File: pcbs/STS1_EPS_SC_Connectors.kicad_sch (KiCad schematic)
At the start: 15 parts, among them J2 Panel Y-, J4 Panel Y+, J5 Panel Z-, J6 Panel Z+, J7 Panel X+, U25 TPS259472ARPW

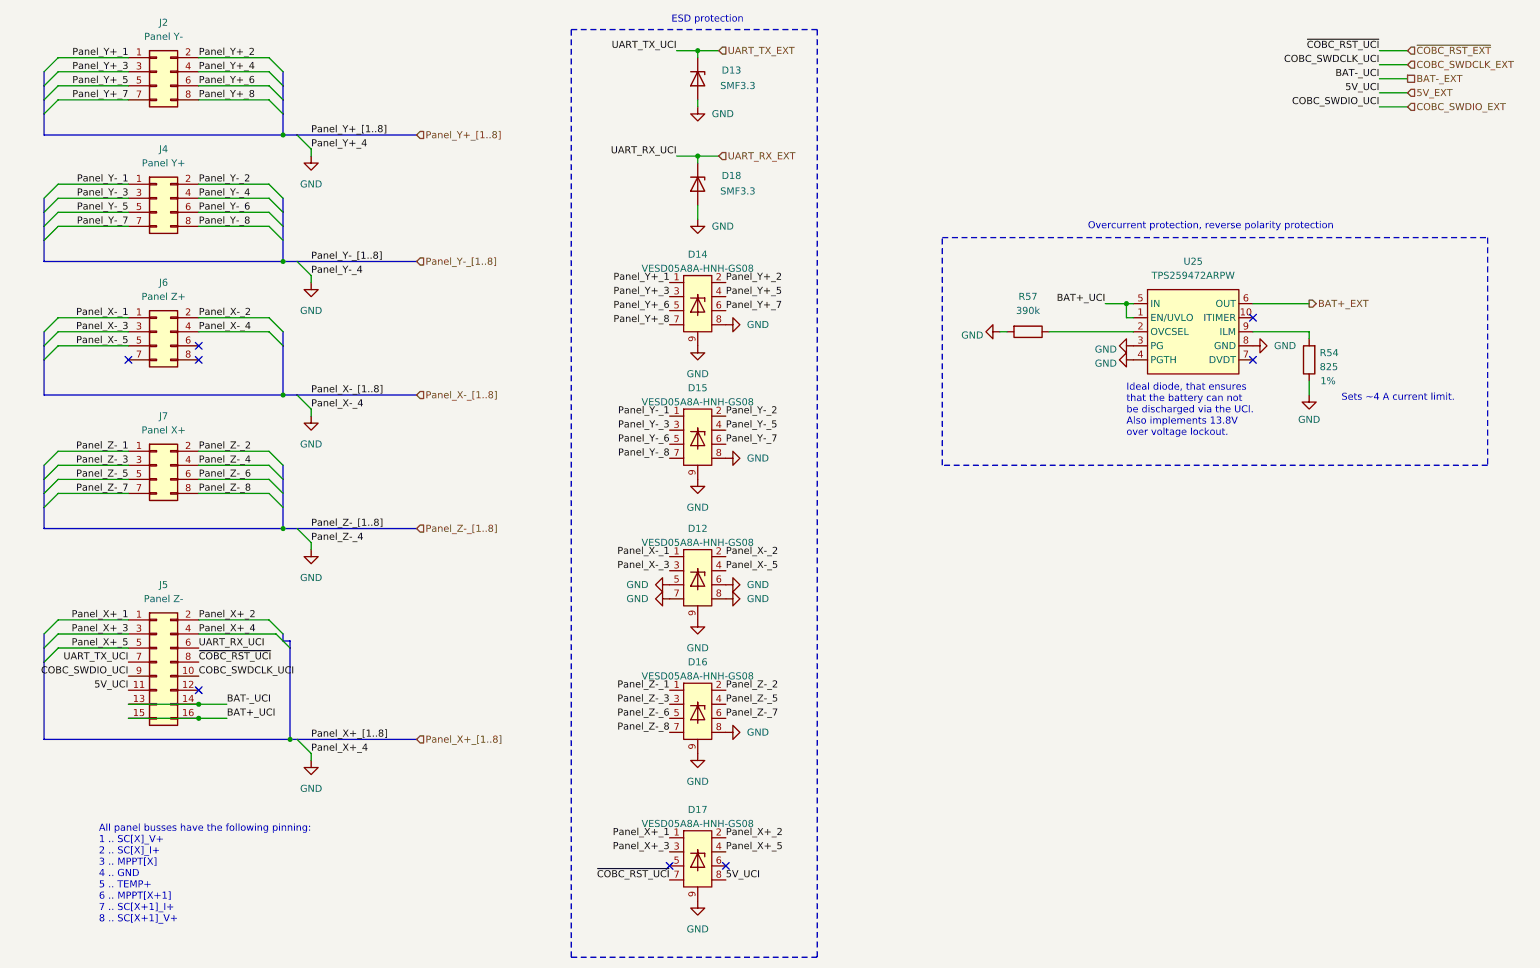
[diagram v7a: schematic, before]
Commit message: Added python script for replacing labels within KiCad.
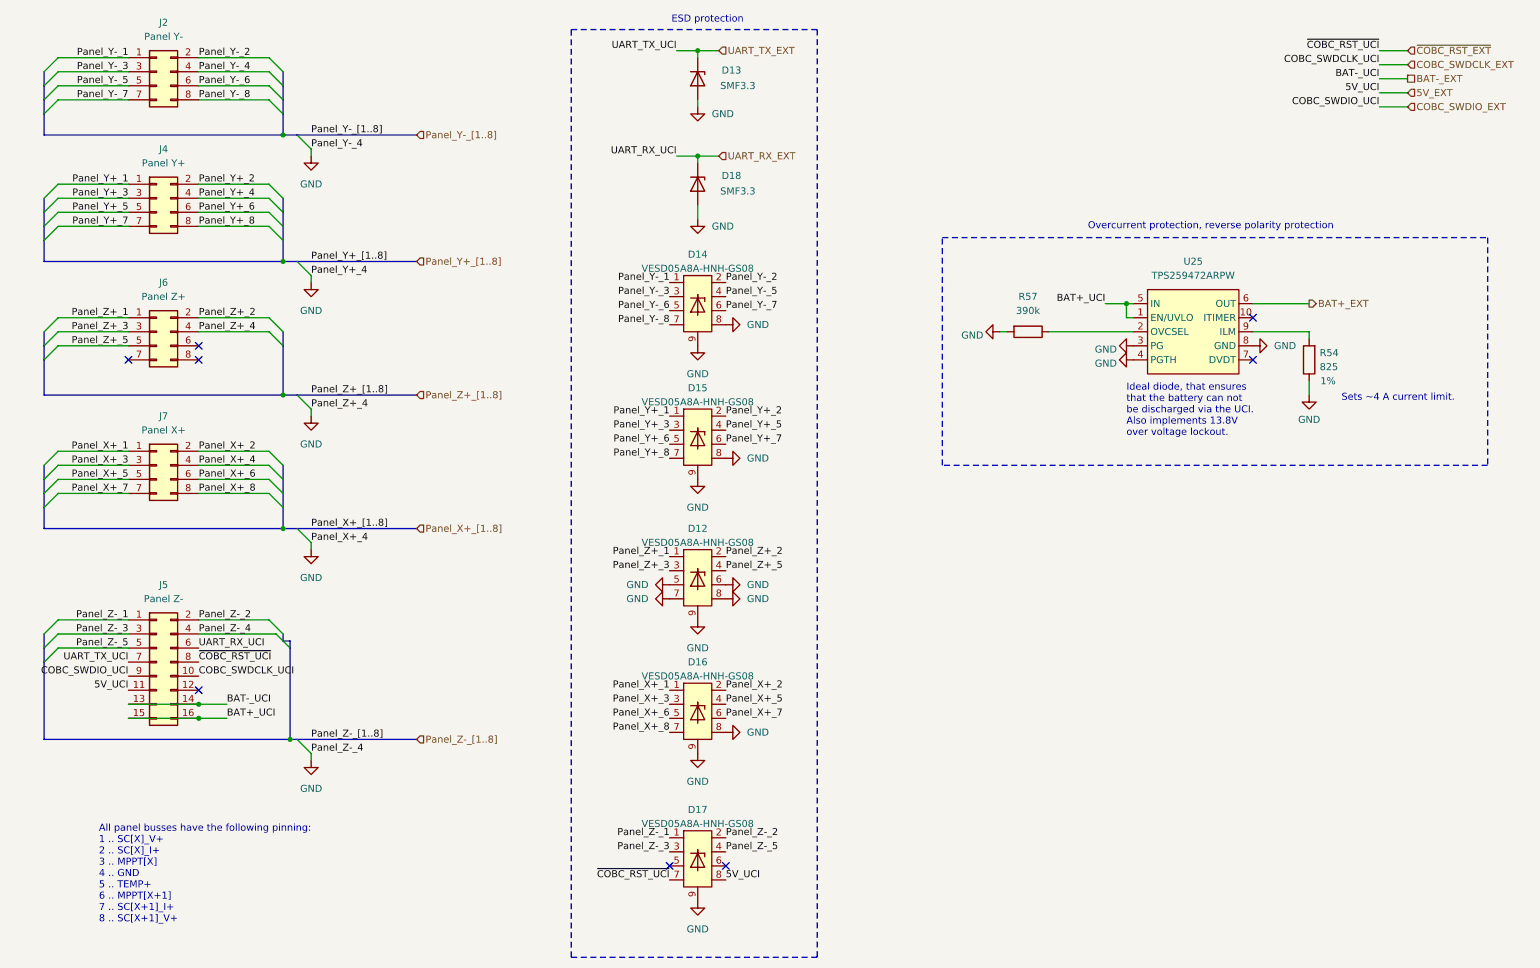
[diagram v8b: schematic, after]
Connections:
- net Panel_X+_1: now also D16.1, J7.1 (Pin_1); no longer D17.1, J5.1 (Pin_1)
- net Panel_X+_2: now also D16.2, J7.2 (Pin_2); no longer D17.2, J5.2 (Pin_2)
- net Panel_X+_3: now also D16.3, J7.3 (Pin_3); no longer D17.3, J5.3 (Pin_3)
- net Panel_X+_5: now also D16.4, J7.5 (Pin_5); no longer D17.4, J5.5 (Pin_5)
- net Panel_Y+_1: now also D15.1, J4.1 (Pin_1); no longer D14.1, J2.1 (Pin_1)
- net Panel_Y+_2: now also D15.2, J4.2 (Pin_2); no longer D14.2, J2.2 (Pin_2)
- net Panel_Y+_3: now also D15.3, J4.3 (Pin_3); no longer D14.3, J2.3 (Pin_3)
- net Panel_Y+_5: now also D15.4, J4.5 (Pin_5); no longer D14.4, J2.5 (Pin_5)
- net Panel_Y+_6: now also D15.5, J4.6 (Pin_6); no longer D14.5, J2.6 (Pin_6)
- net Panel_Y+_7: now also D15.6, J4.7 (Pin_7); no longer D14.6, J2.7 (Pin_7)
- net Panel_Y+_8: now also D15.7, J4.8 (Pin_8); no longer D14.7, J2.8 (Pin_8)
- net Panel_Y-_1: now also D14.1, J2.1 (Pin_1); no longer D15.1, J4.1 (Pin_1)
- net Panel_Y-_2: now also D14.2, J2.2 (Pin_2); no longer D15.2, J4.2 (Pin_2)
- net Panel_Y-_3: now also D14.3, J2.3 (Pin_3); no longer D15.3, J4.3 (Pin_3)
- net Panel_Y-_5: now also D14.4, J2.5 (Pin_5); no longer D15.4, J4.5 (Pin_5)
- net Panel_Y-_6: now also D14.5, J2.6 (Pin_6); no longer D15.5, J4.6 (Pin_6)
- net Panel_Y-_7: now also D14.6, J2.7 (Pin_7); no longer D15.6, J4.7 (Pin_7)
- net Panel_Y-_8: now also D14.7, J2.8 (Pin_8); no longer D15.7, J4.8 (Pin_8)
- net Panel_Z-_1: now also D17.1, J5.1 (Pin_1); no longer D16.1, J7.1 (Pin_1)
- net Panel_Z-_2: now also D17.2, J5.2 (Pin_2); no longer D16.2, J7.2 (Pin_2)
- net Panel_Z-_3: now also D17.3, J5.3 (Pin_3); no longer D16.3, J7.3 (Pin_3)
- net Panel_Z-_5: now also D17.4, J5.5 (Pin_5); no longer D16.4, J7.5 (Pin_5)
- net Panel_X-_1 renamed Panel_Z+_1
- net Panel_X-_2 renamed Panel_Z+_2
- net Panel_X-_3 renamed Panel_Z+_3
- net Panel_X-_5 renamed Panel_Z+_5
- net Panel_Z-_6 renamed Panel_X+_6
- net Panel_Z-_7 renamed Panel_X+_7
- net Panel_Z-_8 renamed Panel_X+_8
